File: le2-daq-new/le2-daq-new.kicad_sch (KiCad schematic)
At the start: 22 parts, among them J1 RELAY-CONN, J10 PWR-RAIL, J11 PWR-RAIL, J12 PWR-RAIL, J13 PWR-RAIL, J14 PWR-RAIL, J15 PWR-RAIL, J16 PWR-RAIL, J2 PT-CONN, J3 TC-CONN, J4 CAP-CONN, J5 PWR-RAIL, J6 PWR-RAIL, J7 PWR-RAIL, J8 PWR-RAIL, J9 PWR-RAIL, U1 ESP32-DEVKITC-32D

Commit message: owo
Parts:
- added J17: Screw_Terminal_01x02, Connector_PinHeader_2.54mm:PinHeader_1x02_P2.54mm_Horizontal, symbol Connector:Screw_Terminal_01x02
- J1: footprint Connector_PinHeader_1.00mm:PinHeader_1x10_P1.00mm_Horizontal -> Connector_PinHeader_2.54mm:PinHeader_1x10_P2.54mm_Horizontal
- J10, J11, J12, J13, J14, J15, J16, J5, J6, J7, J8, J9: footprint Connector_PinHeader_1.00mm:PinHeader_1x02_P1.00mm_Horizontal -> Connector_PinHeader_2.54mm:PinHeader_1x02_P2.54mm_Horizontal
- J2: footprint Connector_PinHeader_1.00mm:PinHeader_1x09_P1.00mm_Horizontal -> Connector_PinHeader_2.54mm:PinHeader_1x09_P2.54mm_Horizontal
- J3: footprint Connector_PinHeader_1.00mm:PinHeader_1x06_P1.00mm_Horizontal -> Connector_PinHeader_2.54mm:PinHeader_1x06_P2.54mm_Horizontal
- J4: footprint Connector_PinHeader_1.00mm:PinHeader_1x05_P1.00mm_Horizontal -> Connector_PinHeader_2.54mm:PinHeader_1x05_P2.54mm_Horizontal
- R2: value 100 -> 5K
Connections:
- net 12V: now also J17.2 (Pin_2)
- net GND: now also J17.1 (Pin_1)

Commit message: stash
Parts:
- removed D1, D2: LED, LED_THT:LED_D3.0mm, symbol Device:LED
- removed J10, J11, J12, J13, J14, J15, J16, J6, J7, J8, J9: PWR-RAIL, Connector_PinHeader_2.54mm:PinHeader_1x02_P2.54mm_Horizontal, symbol Connector:Conn_01x02_Male
- removed J17: Screw_Terminal_01x02, Connector_PinHeader_2.54mm:PinHeader_1x02_P2.54mm_Horizontal, symbol Connector:Screw_Terminal_01x02
- removed J2: PT-CONN, Connector_PinHeader_2.54mm:PinHeader_1x09_P2.54mm_Horizontal, symbol Connector:Conn_01x08_Male
- removed J3: TC-CONN, Connector_PinHeader_2.54mm:PinHeader_1x06_P2.54mm_Horizontal, symbol Connector:Conn_01x06_Male
- removed J4: CAP-CONN, Connector_PinHeader_2.54mm:PinHeader_1x05_P2.54mm_Horizontal, symbol Connector:Conn_01x05_Male
- removed R2: 5K, Resistor_SMD:R_0805_2012Metric_Pad1.20x1.40mm_HandSolder, symbol Device:R_Small
- removed R3: 100, Resistor_SMD:R_0805_2012Metric_Pad1.20x1.40mm_HandSolder, symbol Device:R_Small
- added J2: CAP-CONN, PCIE_1x_Socket:AMPHENOL_10018784-10210TLF, symbol Connector_Generic:Conn_02x18_Row_Letter_First
- added J3: TC-CONN, PCIE_1x_Socket:AMPHENOL_10018784-10210TLF, symbol Connector_Generic:Conn_02x18_Row_Letter_First
- added J4: HX_CON, PCIE_1x_Socket:AMPHENOL_10018784-10210TLF, symbol Connector_Generic:Conn_02x18_Row_Letter_First
- added SW1: SW_Push, Jumper:SolderJumper-2_P1.3mm_Bridged2Bar_Pad1.0x1.5mm, symbol Switch:SW_Push
- J1: footprint Connector_PinHeader_2.54mm:PinHeader_1x10_P2.54mm_Horizontal -> PCIE_1x_Socket:AMPHENOL_10018784-10210TLF; symbol Connector:Conn_01x10_Male -> Connector_Generic:Conn_02x18_Row_Letter_First
- J5: value PWR-RAIL -> Conn_01x02_Male
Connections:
- net PT 1 is gone; now on net TC CLK: U1.3 (SENSOR_VP)
- net PT 2 is gone; now on net TC SDO: U1.4 (SENSOR_VN)
- net PT 3 is gone; now on net TC1 CS: U1.5 (IO34)
- net PT 4 is gone; now on net TC2 CS: U1.6 (IO35)
- net +3.3V: now also J1.A1 (Pin_a1), J2.A1 (Pin_a1), J3.A1 (Pin_a1), J4.A1 (Pin_a1); no longer J1.9 (Pin_9)
- net GND: now also J1.A2 (Pin_a2), J2.A2 (Pin_a2), J3.A2 (Pin_a2), J4.A2 (Pin_a2); no longer J1.10 (Pin_10)
- net RL 1: now also J1.B1 (Pin_b1); no longer J1.1 (Pin_1)
- net RL 2: now also J1.B2 (Pin_b2); no longer J1.2 (Pin_2)
- net RL 3: now also J1.B3 (Pin_b3); no longer J1.3 (Pin_3)
- net RL 4: now also J1.B4 (Pin_b4); no longer J1.4 (Pin_4)
- net RL 5: now also J1.B5 (Pin_b5); no longer J1.5 (Pin_5)
- net RL 6: now also J1.B6 (Pin_b6); no longer J1.6 (Pin_6)
- net RL 7: now also J1.B7 (Pin_b7); no longer J1.7 (Pin_7)
- net RL 8: now also J1.B8 (Pin_b8); no longer J1.8 (Pin_8)
- net TC CLK: now also J3.B4 (Pin_b4); no longer U1.32 (IO4)
- net TC SDO: now also J3.B3 (Pin_b3); no longer U1.10 (IO26)
- net TC1 CS: now also J3.B2 (Pin_b2); no longer U1.8 (IO33)
- net TC2 CS: now also J3.B1 (Pin_b1); no longer U1.9 (IO25)
- net at R1.1: now also SW1.1; no longer U1.2 (EN)
- net CAP 1: now reaches U1.16 (SD2)
- net CAP 1: now also J2.B1 (Pin_b1)
- net CAP 2: now reaches U1.17 (SD3)
- net CAP 2: now also J2.B2 (Pin_b2)
- net CS 1 renamed HX CLK
- net HX CLK: now also J4.B6 (Pin_b6)
- net CS 2: no longer names the net of U1.15 (IO13)
- net CS CLK renamed CAP CLK
- net CAP CLK: now also J2.B3 (Pin_b3)
- net PT 5 renamed HXPT 1
- net HXPT 1: now also J4.B1 (Pin_b1)
- net PT CLK renamed HXLC 2
- net HXLC 2: now also J4.B5 (Pin_b5)
- new net: SW1.2, U1.2 (EN)
- new net HXLC 1: J4.B4 (Pin_b4), U1.10 (IO26)
- new net HXPT 2: J4.B2 (Pin_b2), U1.8 (IO33)
- new net HXPT 3: J4.B3 (Pin_b3), U1.9 (IO25)
- no-connect marks 12 -> 127
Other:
- moved on the sheet: R1, U1

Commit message: CORE PCB DONE
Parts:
- added J6, J7: TEST-POINT, Connector_PinHeader_2.54mm:PinHeader_1x19_P2.54mm_Horizontal, symbol Connector:Conn_01x19_Male
- J1: value RELAY-CONN -> PCIE_CONN; footprint PCIE_1x_Socket:AMPHENOL_10018784-10210TLF -> PCIE-LP-01-01-F-DV-A-TR:SAMTEC_PCIE-LP-01-01-F-DV-A-TR
- J2: value CAP-CONN -> PCIE_CONN; footprint PCIE_1x_Socket:AMPHENOL_10018784-10210TLF -> PCIE-LP-01-01-F-DV-A-TR:SAMTEC_PCIE-LP-01-01-F-DV-A-TR
- J3: value TC-CONN -> PCIE_CONN; footprint PCIE_1x_Socket:AMPHENOL_10018784-10210TLF -> PCIE-LP-01-01-F-DV-A-TR:SAMTEC_PCIE-LP-01-01-F-DV-A-TR
- J4: value HX_CON -> PCIE_CONN; footprint PCIE_1x_Socket:AMPHENOL_10018784-10210TLF -> PCIE-LP-01-01-F-DV-A-TR:SAMTEC_PCIE-LP-01-01-F-DV-A-TR
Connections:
- net +3.3V: now also J1.B17 (Pin_b17), J1.B18 (Pin_b18), J2.B17 (Pin_b17), J2.B18 (Pin_b18), J3.B17 (Pin_b17), J3.B18 (Pin_b18), J4.B17 (Pin_b17), J4.B18 (Pin_b18), J7.19 (Pin_19); no longer J1.A1 (Pin_a1), J2.A1 (Pin_a1), J3.A1 (Pin_a1), J4.A1 (Pin_a1)
- net CAP 1: now also J1.B13 (Pin_b13), J2.B13 (Pin_b13), J3.B13 (Pin_b13), J4.B13 (Pin_b13), J7.4 (Pin_4); no longer J2.B1 (Pin_b1)
- net CAP 2: now also J1.A12 (Pin_a12), J2.A12 (Pin_a12), J3.A12 (Pin_a12), J4.A12 (Pin_a12), J7.3 (Pin_3); no longer J2.B2 (Pin_b2)
- net CAP CLK: now also J1.B15 (Pin_b15), J2.B15 (Pin_b15), J3.B15 (Pin_b15), J4.B15 (Pin_b15), U1.38 (CLK), J6.19 (Pin_19); no longer J2.B3 (Pin_b3), U1.35 (IO15)
- net GND: now also J1.A10 (Pin_a10), J1.A14 (Pin_a14), J1.A15 (Pin_a15), J1.A4 (Pin_a4), J1.A7 (Pin_a7), J1.B12 (Pin_b12), J1.B16 (Pin_b16), J1.B2 (Pin_b2), J1.B6 (Pin_b6), J1.B9 (Pin_b9), J2.A10 (Pin_a10), J2.A14 (Pin_a14), J2.A15 (Pin_a15), J2.A4 (Pin_a4), J2.A7 (Pin_a7), J2.B12 (Pin_b12), J2.B16 (Pin_b16), J2.B2 (Pin_b2), J2.B6 (Pin_b6), J2.B9 (Pin_b9), J3.A10 (Pin_a10), J3.A14 (Pin_a14), J3.A15 (Pin_a15), J3.A4 (Pin_a4), J3.A7 (Pin_a7), J3.B12 (Pin_b12), J3.B16 (Pin_b16), J3.B2 (Pin_b2), J3.B6 (Pin_b6), J3.B9 (Pin_b9), J4.A10 (Pin_a10), J4.A14 (Pin_a14), J4.A15 (Pin_a15), J4.A4 (Pin_a4), J4.A7 (Pin_a7), J4.B12 (Pin_b12), J4.B16 (Pin_b16), J4.B2 (Pin_b2), J4.B6 (Pin_b6), J4.B9 (Pin_b9), J6.1 (Pin_1), J6.7 (Pin_7), J7.6 (Pin_6)
- net HX CLK: now also J1.A11 (Pin_a11), J2.A11 (Pin_a11), J3.A11 (Pin_a11), J4.A11 (Pin_a11), U1.11 (IO27), J7.9 (Pin_9); no longer J4.B6 (Pin_b6), U1.12 (IO14)
- net TC CLK: now also J1.B5 (Pin_b5), J2.B5 (Pin_b5), J3.B5 (Pin_b5), J4.B5 (Pin_b5), U1.31 (IO16), J6.12 (Pin_12); no longer J3.B4 (Pin_b4), U1.3 (SENSOR_VP)
- net TC SDO: now also J1.A3 (Pin_a3), J2.A3 (Pin_a3), J3.A3 (Pin_a3), J4.A3 (Pin_a3), U1.30 (IO17), J6.11 (Pin_11); no longer J3.B3 (Pin_b3), U1.4 (SENSOR_VN)
- net TC1 CS: now also J1.B3 (Pin_b3), J2.B3 (Pin_b3), J3.B3 (Pin_b3), J4.B3 (Pin_b3), U1.29 (IO5), J6.10 (Pin_10); no longer J3.B2 (Pin_b2), U1.5 (IO34)
- net TC2 CS: now also J1.B4 (Pin_b4), J2.B4 (Pin_b4), J3.B4 (Pin_b4), J4.B4 (Pin_b4), U1.28 (IO18), J6.9 (Pin_9); no longer J3.B1 (Pin_b1), U1.6 (IO35)
- net +5V: now reaches U1.19 (EXT_5V)
- net +5V: now also J1.A17 (Pin_a17), J1.A18 (Pin_a18), J2.A17 (Pin_a17), J2.A18 (Pin_a18), J3.A17 (Pin_a17), J3.A18 (Pin_a18), J4.A17 (Pin_a17), J4.A18 (Pin_a18), J7.1 (Pin_1)
- net EN: now reaches SW1.2, U1.2 (EN)
- net EN: now also J7.18 (Pin_18)
- net PHOTORES: now reaches J3.A13 (Pin_a13)
- net PHOTORES: now also J1.A13 (Pin_a13), J2.A13 (Pin_a13), J4.A13 (Pin_a13), U1.27 (IO19), J6.8 (Pin_8)
- net EXTRA: now reaches J3.A16 (Pin_a16)
- net EXTRA: now also J1.A16 (Pin_a16), J2.A16 (Pin_a16), J4.A16 (Pin_a16), U1.12 (IO14), J7.8 (Pin_8)
- net HX 1: now reaches J3.A5 (Pin_a5)
- net HX 1: now also J1.A5 (Pin_a5), J2.A5 (Pin_a5), J4.A5 (Pin_a5), U1.3 (SENSOR_VP), J7.17 (Pin_17)
- net HX 3: now reaches J3.A6 (Pin_a6)
- net HX 3: now also J1.A6 (Pin_a6), J2.A6 (Pin_a6), J4.A6 (Pin_a6), U1.5 (IO34), J7.15 (Pin_15)
- net HX 5: now reaches J3.A8 (Pin_a8)
- net HX 5: now also J1.A8 (Pin_a8), J2.A8 (Pin_a8), J4.A8 (Pin_a8), U1.7 (IO32), J7.13 (Pin_13)
- net HX 7: now reaches J3.A9 (Pin_a9)
- net HX 7: now also J1.A9 (Pin_a9), J2.A9 (Pin_a9), J4.A9 (Pin_a9), U1.9 (IO25), J7.11 (Pin_11)
- net HX 6: now reaches J3.B10 (Pin_b10)
- net HX 6: now also J1.B10 (Pin_b10), J2.B10 (Pin_b10), J4.B10 (Pin_b10), U1.8 (IO33), J7.12 (Pin_12)
- net HX 8: now reaches J3.B11 (Pin_b11)
- net HX 8: now also J1.B11 (Pin_b11), J2.B11 (Pin_b11), J4.B11 (Pin_b11), U1.10 (IO26), J7.10 (Pin_10)
- net RL INT: now reaches J3.B14 (Pin_b14)
- net RL INT: now also J1.B14 (Pin_b14), J2.B14 (Pin_b14), J4.B14 (Pin_b14), U1.21 (IO23), J6.2 (Pin_2)
- net HX 2: now reaches J3.B7 (Pin_b7)
- net HX 2: now also J1.B7 (Pin_b7), J2.B7 (Pin_b7), J4.B7 (Pin_b7), U1.4 (SENSOR_VN), J7.16 (Pin_16)
- net HX 4: now reaches J3.B8 (Pin_b8)
- net HX 4: now also J1.B8 (Pin_b8), J2.B8 (Pin_b8), J4.B8 (Pin_b8), U1.6 (IO35), J7.14 (Pin_14)
- removed net HXLC 1: J4.B4 (Pin_b4), U1.10 (IO26)
- removed net HXLC 2: J4.B5 (Pin_b5), U1.11 (IO27)
- net HXPT 1 renamed RL SCL
- net RL SCL: now also J1.B1 (Pin_b1), J2.B1 (Pin_b1), J3.B1 (Pin_b1), U1.22 (IO22), J6.3 (Pin_3); no longer U1.7 (IO32)
- removed net HXPT 2: J4.B2 (Pin_b2), U1.8 (IO33)
- removed net HXPT 3: J4.B3 (Pin_b3), U1.9 (IO25)
- removed net RL 1: J1.B1 (Pin_b1), U1.21 (IO23)
- removed net RL 2: J1.B2 (Pin_b2), U1.22 (IO22)
- net RL 3 renamed RL SDA
- net RL SDA: now also J1.A1 (Pin_a1), J2.A1 (Pin_a1), J3.A1 (Pin_a1), J4.A1 (Pin_a1), J6.6 (Pin_6); no longer J1.B3 (Pin_b3)
- removed net RL 4: J1.B4 (Pin_b4), U1.27 (IO19)
- removed net RL 5: J1.B5 (Pin_b5), U1.28 (IO18)
- removed net RL 6: J1.B6 (Pin_b6), U1.29 (IO5)
- removed net RL 7: J1.B7 (Pin_b7), U1.30 (IO17)
- removed net RL 8: J1.B8 (Pin_b8), U1.31 (IO16)
- no-connect marks 127 -> 22
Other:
- note added: "ESP32"
- note added: "External Power Input"
- note added: "PCIE Card Edge Connectors - Plug and Play Any board can use any slot"
- note added: "Pullup Resistor circuit - EN"
- note added: "Test Points"
- moved on the sheet: J1, J5, U1

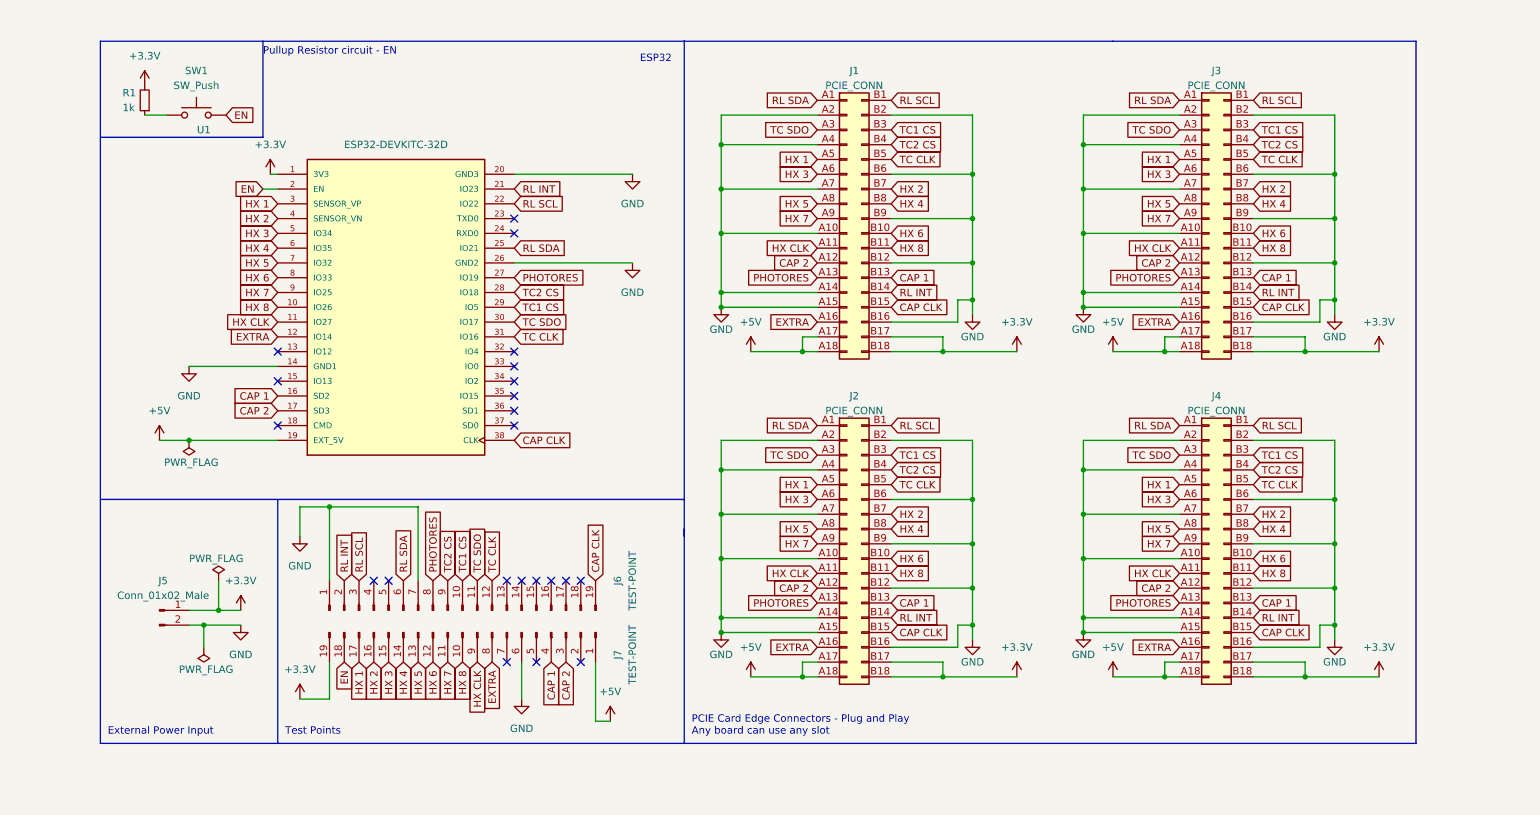
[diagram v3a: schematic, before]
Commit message: new daq layout
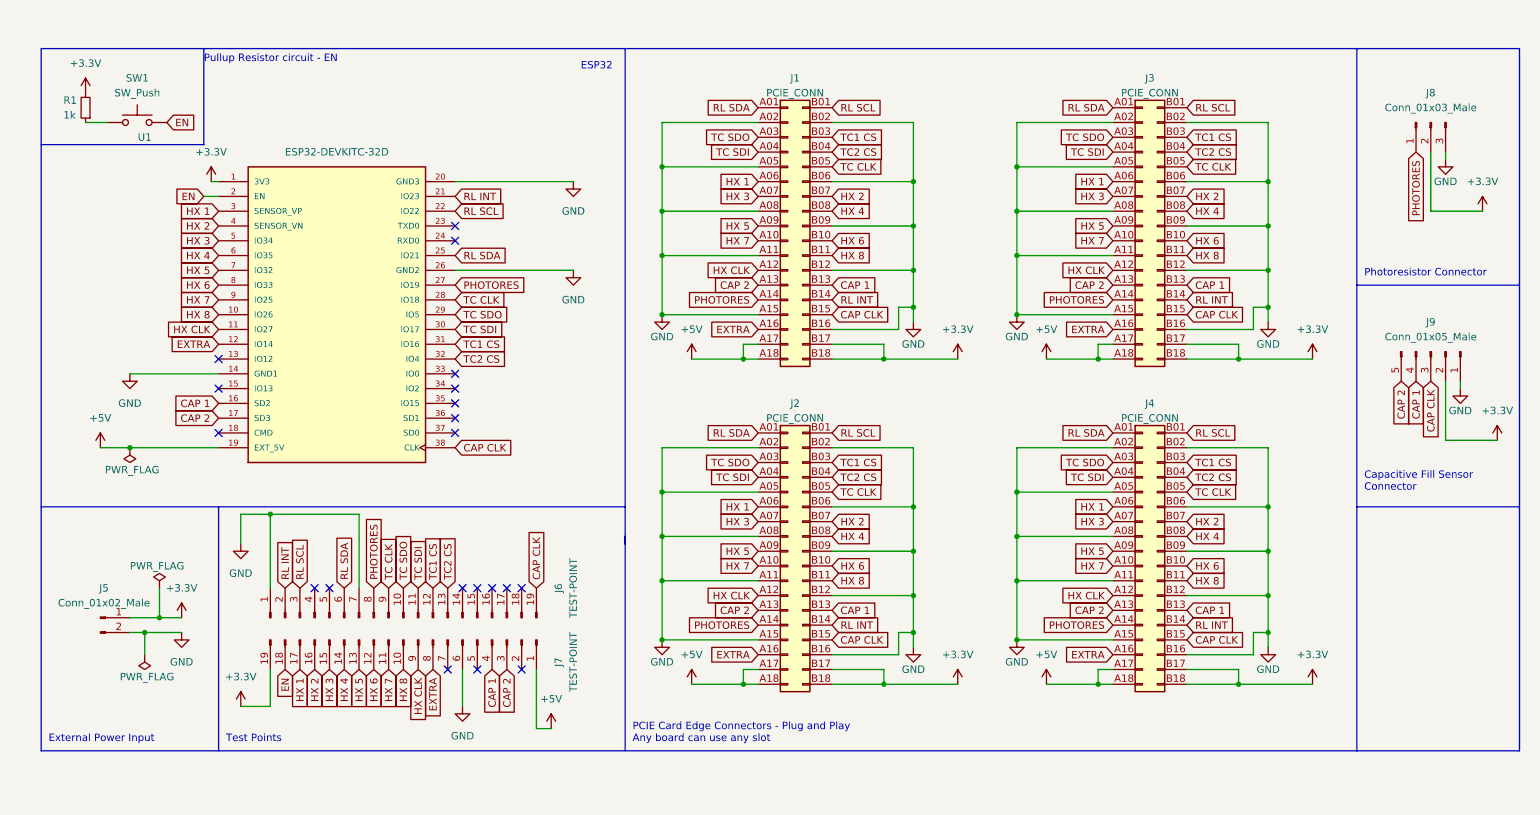
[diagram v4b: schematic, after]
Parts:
- added J8: Conn_01x03_Male, Connector_PinHeader_2.54mm:PinHeader_1x03_P2.54mm_Vertical, symbol Connector:Conn_01x03_Male
- added J9: Conn_01x05_Male, Connector_PinHeader_2.54mm:PinHeader_1x05_P2.54mm_Vertical, symbol Connector:Conn_01x05_Male
- J5: footprint Connector_PinHeader_2.54mm:PinHeader_1x02_P2.54mm_Horizontal -> Connector_PinHeader_2.54mm:PinHeader_1x02_P2.54mm_Vertical
- J6, J7: footprint Connector_PinHeader_2.54mm:PinHeader_1x19_P2.54mm_Horizontal -> Connector_PinHeader_2.54mm:PinHeader_1x19_P2.54mm_Vertical
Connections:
- net +3.3V: now also J8.2 (Pin_2), J9.2 (Pin_2)
- net CAP 1: now also J9.4 (Pin_4)
- net CAP 2: now also J1.A13 (Pin_a13), J2.A13 (Pin_a13), J3.A13 (Pin_a13), J4.A13 (Pin_a13), J9.5 (Pin_5); no longer J1.A12 (Pin_a12), J2.A12 (Pin_a12), J3.A12 (Pin_a12), J4.A12 (Pin_a12)
- net CAP CLK: now also J9.3 (Pin_3)
- net GND: now also J1.A02 (Pin_a2), J1.A05 (Pin_a5), J1.A08 (Pin_a8), J1.A11 (Pin_a11), J1.B02 (Pin_b2), J1.B06 (Pin_b6), J1.B09 (Pin_b9), J2.A02 (Pin_a2), J2.A05 (Pin_a5), J2.A08 (Pin_a8), J2.A11 (Pin_a11), J2.B02 (Pin_b2), J2.B06 (Pin_b6), J2.B09 (Pin_b9), J3.A02 (Pin_a2), J3.A05 (Pin_a5), J3.A08 (Pin_a8), J3.A11 (Pin_a11), J3.B02 (Pin_b2), J3.B06 (Pin_b6), J3.B09 (Pin_b9), J4.A02 (Pin_a2), J4.A05 (Pin_a5), J4.A08 (Pin_a8), J4.A11 (Pin_a11), J4.B02 (Pin_b2), J4.B06 (Pin_b6), J4.B09 (Pin_b9), J8.3 (Pin_3), J9.1 (Pin_1); no longer J1.A10 (Pin_a10), J1.A14 (Pin_a14), J1.A2 (Pin_a2), J1.A4 (Pin_a4), J1.A7 (Pin_a7), J1.B2 (Pin_b2), J1.B6 (Pin_b6), J1.B9 (Pin_b9), J2.A10 (Pin_a10), J2.A14 (Pin_a14), J2.A2 (Pin_a2), J2.A4 (Pin_a4), J2.A7 (Pin_a7), J2.B2 (Pin_b2), J2.B6 (Pin_b6), J2.B9 (Pin_b9), J3.A10 (Pin_a10), J3.A14 (Pin_a14), J3.A2 (Pin_a2), J3.A4 (Pin_a4), J3.A7 (Pin_a7), J3.B2 (Pin_b2), J3.B6 (Pin_b6), J3.B9 (Pin_b9), J4.A10 (Pin_a10), J4.A14 (Pin_a14), J4.A2 (Pin_a2), J4.A4 (Pin_a4), J4.A7 (Pin_a7), J4.B2 (Pin_b2), J4.B6 (Pin_b6), J4.B9 (Pin_b9)
- net HX 1: now also J1.A06 (Pin_a6), J2.A06 (Pin_a6), J3.A06 (Pin_a6), J4.A06 (Pin_a6); no longer J1.A5 (Pin_a5), J2.A5 (Pin_a5), J3.A5 (Pin_a5), J4.A5 (Pin_a5)
- net HX 2: now also J1.B07 (Pin_b7), J2.B07 (Pin_b7), J3.B07 (Pin_b7), J4.B07 (Pin_b7); no longer J1.B7 (Pin_b7), J2.B7 (Pin_b7), J3.B7 (Pin_b7), J4.B7 (Pin_b7)
- net HX 3: now also J1.A07 (Pin_a7), J2.A07 (Pin_a7), J3.A07 (Pin_a7), J4.A07 (Pin_a7); no longer J1.A6 (Pin_a6), J2.A6 (Pin_a6), J3.A6 (Pin_a6), J4.A6 (Pin_a6)
- net HX 4: now also J1.B08 (Pin_b8), J2.B08 (Pin_b8), J3.B08 (Pin_b8), J4.B08 (Pin_b8); no longer J1.B8 (Pin_b8), J2.B8 (Pin_b8), J3.B8 (Pin_b8), J4.B8 (Pin_b8)
- net HX 5: now also J1.A09 (Pin_a9), J2.A09 (Pin_a9), J3.A09 (Pin_a9), J4.A09 (Pin_a9); no longer J1.A8 (Pin_a8), J2.A8 (Pin_a8), J3.A8 (Pin_a8), J4.A8 (Pin_a8)
- net HX 7: now also J1.A10 (Pin_a10), J2.A10 (Pin_a10), J3.A10 (Pin_a10), J4.A10 (Pin_a10); no longer J1.A9 (Pin_a9), J2.A9 (Pin_a9), J3.A9 (Pin_a9), J4.A9 (Pin_a9)
- net HX CLK: now also J1.A12 (Pin_a12), J2.A12 (Pin_a12), J3.A12 (Pin_a12), J4.A12 (Pin_a12); no longer J1.A11 (Pin_a11), J2.A11 (Pin_a11), J3.A11 (Pin_a11), J4.A11 (Pin_a11)
- net PHOTORES: now also J1.A14 (Pin_a14), J2.A14 (Pin_a14), J3.A14 (Pin_a14), J4.A14 (Pin_a14), J8.1 (Pin_1); no longer J1.A13 (Pin_a13), J2.A13 (Pin_a13), J3.A13 (Pin_a13), J4.A13 (Pin_a13)
- net RL SCL: now also J1.B01 (Pin_b1), J2.B01 (Pin_b1), J3.B01 (Pin_b1), J4.B01 (Pin_b1); no longer J1.B1 (Pin_b1), J2.B1 (Pin_b1), J3.B1 (Pin_b1), J4.B1 (Pin_b1)
- net RL SDA: now also J1.A01 (Pin_a1), J2.A01 (Pin_a1), J3.A01 (Pin_a1), J4.A01 (Pin_a1); no longer J1.A1 (Pin_a1), J2.A1 (Pin_a1), J3.A1 (Pin_a1), J4.A1 (Pin_a1)
- net TC CLK: now also J1.B05 (Pin_b5), J2.B05 (Pin_b5), J3.B05 (Pin_b5), J4.B05 (Pin_b5), J6.9 (Pin_9), U1.28 (IO18); no longer J1.B5 (Pin_b5), J2.B5 (Pin_b5), J3.B5 (Pin_b5), J4.B5 (Pin_b5), J6.12 (Pin_12), U1.31 (IO16)
- net TC SDO: now also J1.A03 (Pin_a3), J2.A03 (Pin_a3), J3.A03 (Pin_a3), J4.A03 (Pin_a3), J6.10 (Pin_10), U1.29 (IO5); no longer J1.A3 (Pin_a3), J2.A3 (Pin_a3), J3.A3 (Pin_a3), J4.A3 (Pin_a3), J6.11 (Pin_11), U1.30 (IO17)
- net TC1 CS: now also J1.B03 (Pin_b3), J2.B03 (Pin_b3), J3.B03 (Pin_b3), J4.B03 (Pin_b3), J6.12 (Pin_12), U1.31 (IO16); no longer J1.B3 (Pin_b3), J2.B3 (Pin_b3), J3.B3 (Pin_b3), J4.B3 (Pin_b3), J6.10 (Pin_10), U1.29 (IO5)
- net TC2 CS: now also J1.B04 (Pin_b4), J2.B04 (Pin_b4), J3.B04 (Pin_b4), J4.B04 (Pin_b4), J6.13 (Pin_13), U1.32 (IO4); no longer J1.B4 (Pin_b4), J2.B4 (Pin_b4), J3.B4 (Pin_b4), J4.B4 (Pin_b4), J6.9 (Pin_9), U1.28 (IO18)
- new net TC SDI: J1.A04 (Pin_a4), J2.A04 (Pin_a4), J3.A04 (Pin_a4), J4.A04 (Pin_a4), J6.11 (Pin_11), U1.30 (IO17)
- no-connect marks 22 -> 20
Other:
- note added: "Capacitive Fill Sensor Connector"
- note added: "Photoresistor Connector"
- moved on the sheet: J1, J5, J6, J7, R1, SW1, U1
